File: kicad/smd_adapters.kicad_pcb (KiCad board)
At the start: 2 copper layers, 79.8 x 69.6 mm, 26 parts

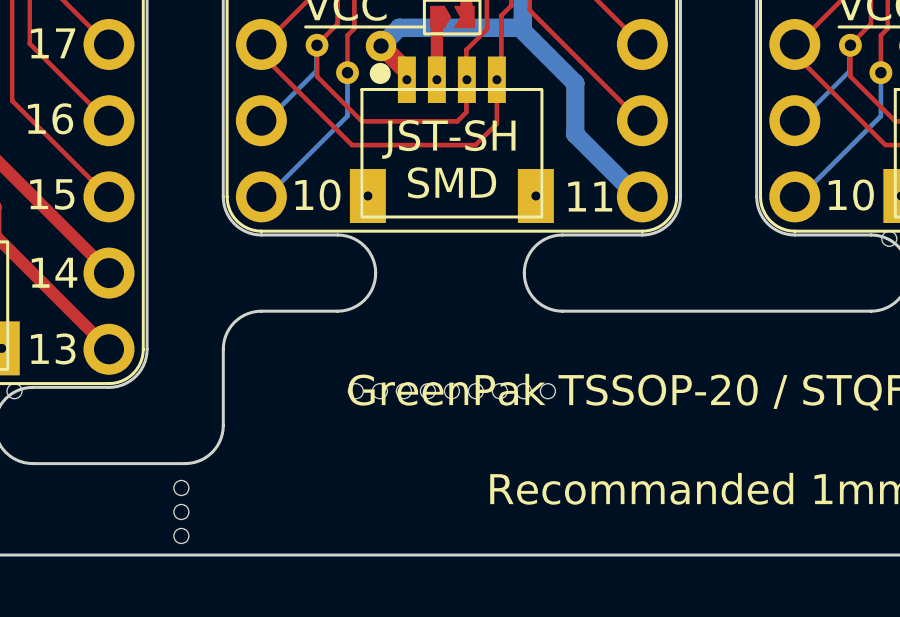
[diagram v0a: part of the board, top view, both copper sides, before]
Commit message: Fixed the mouse bites and regenerated gerbers.
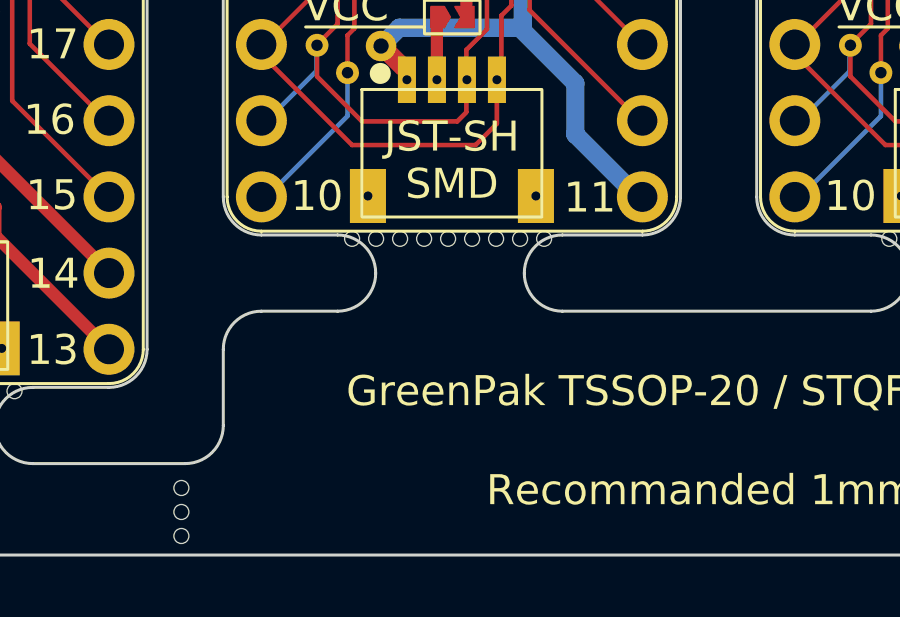
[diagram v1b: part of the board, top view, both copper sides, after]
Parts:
- moved mouse-bite-2.54mm-slot 5.08 mm to (12.1, 20.8)
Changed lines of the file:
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@@
   )
   (footprint "greenpack_smd_adapters:mouse-bite-holes-half" (layer "F.Cu")
-    (at 12.192 25.908 180)
+    (at 12.065 20.828 180)
     (attr through_hole)
     (fp_text reference "mouse-bite-2.54mm-slot" (at 0 -2 180) (layer "F.SilkS") hide
